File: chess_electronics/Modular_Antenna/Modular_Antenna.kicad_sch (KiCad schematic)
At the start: 11 parts, among them J1 Screw_Terminal_01x16, J2 Conn_02x04_Counter_Clockwise, U1 SN74LV4051AN

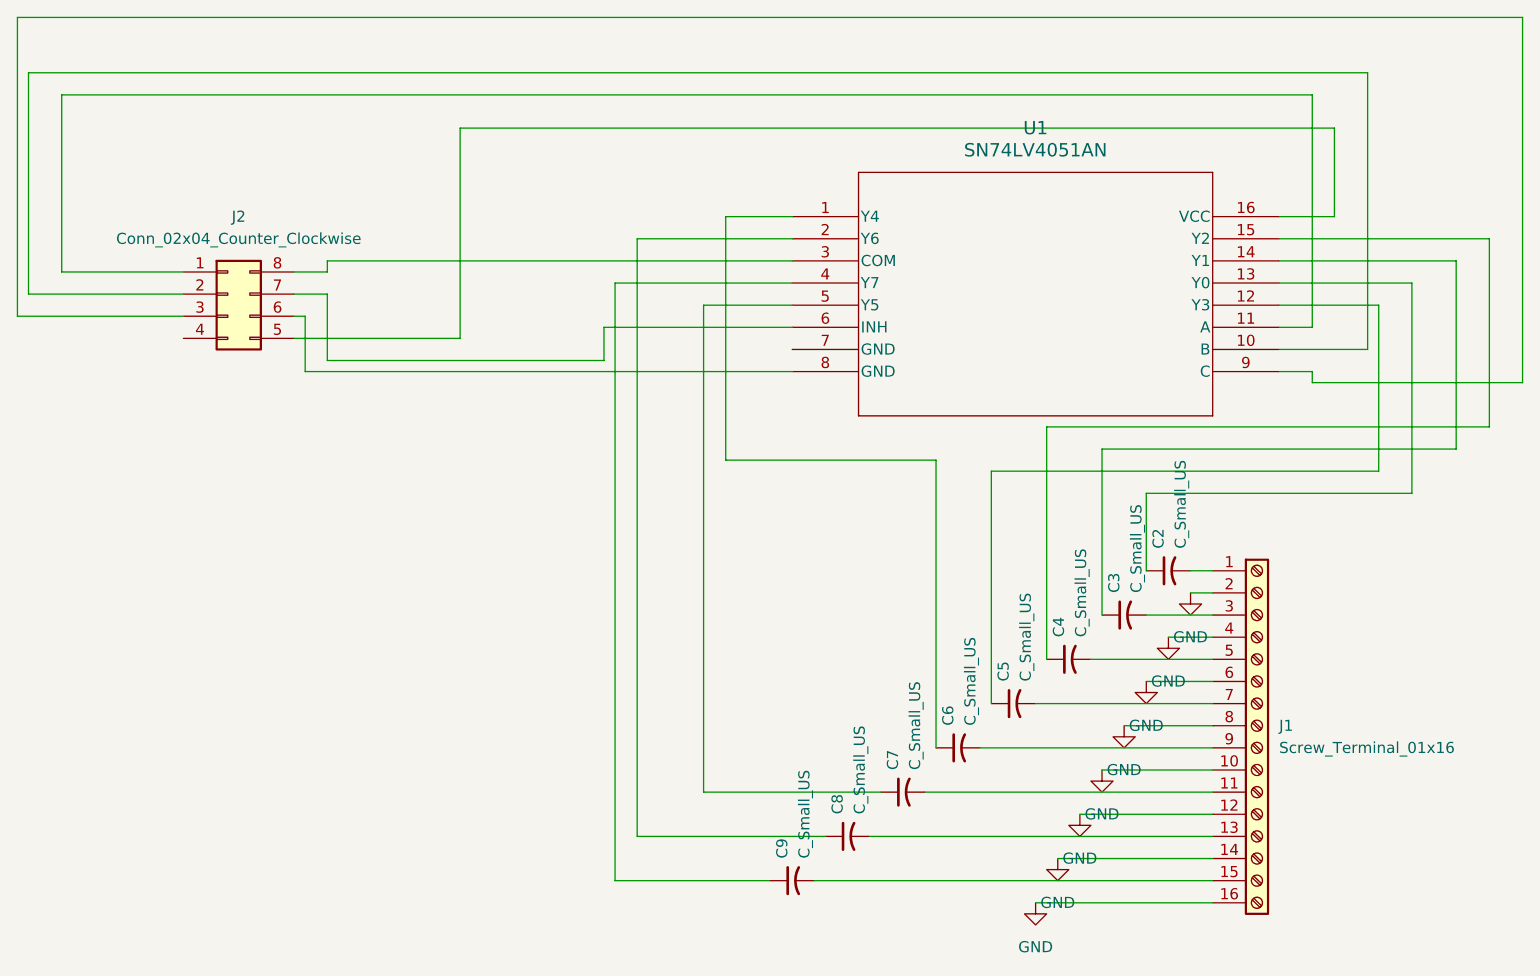
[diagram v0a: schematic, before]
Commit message: Add normally closed relay to modular antenna design
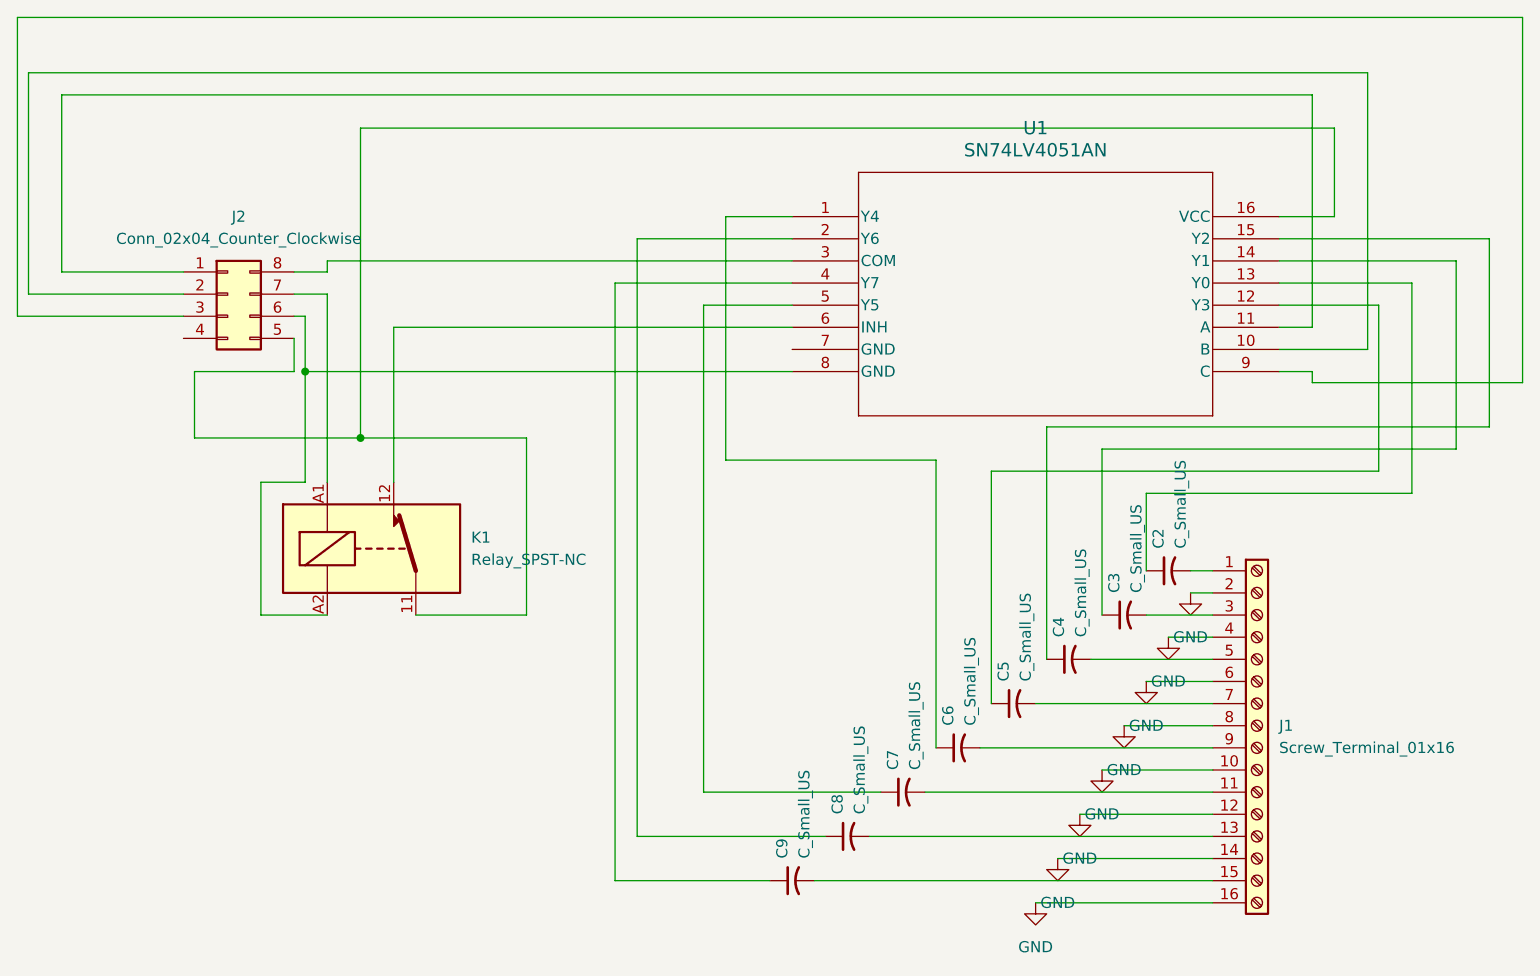
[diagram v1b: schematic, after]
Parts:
- added K1: Relay_SPST-NC, Relay_THT:Relay_SPST_Zettler-AZSR131, symbol Relay:Relay_SPST-NC
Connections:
- net at J2.5 (Pin_5), U1.16 (VCC): now also K1.11
- net at U1.6 (INH): now also K1.12; no longer J2.7 (Pin_7)
- net at J2.6 (Pin_6), U1.8 (GND): now also K1.A2
- new net: J2.7 (Pin_7), K1.A1
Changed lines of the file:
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@@
 	(generator_version "9.0")
 	(paper "A4")
+	(junction
+		(at 55.88 95.25)
+		(diameter 0)
+		(color 0 0 0 0)
+	)
+	(junction
+		(at 49.53 87.63)
+		(diameter 0)
+		(color 0 0 0 0)
+	)
 	(wire
 		(pts
@@
 	(wire
 		(pts
+			(xy 36.83 95.25) (xy 36.83 87.63)
+		)
+		(stroke
+			(width 0)
+			(type default)
+		)
+	)
+	(wire
+		(pts
 			(xy 171.45 53.34) (xy 17.78 53.34)
 		)
@@
 	(wire
 		(pts
+			(xy 55.88 95.25) (xy 74.93 95.25)
+		)
+		(stroke
+			(width 0)
+			(type default)
+		)
+	)
+	(wire
+		(pts
 			(xy 143.51 128.27) (xy 153.67 128.27)
 		)
@@
 	(wire
 		(pts
+			(xy 36.83 87.63) (xy 48.26 87.63)
+		)
+		(stroke
+			(width 0)
+			(type default)
+		)
+	)
+	(wire
+		(pts
 			(xy 151.13 110.49) (xy 153.67 110.49)
 		)
@@
 	(wire
 		(pts
+			(xy 52.07 100.33) (xy 52.07 78.74)
+		)
+		(stroke
+			(width 0)
+			(type default)
+		)
+	)
+	(wire
+		(pts
 			(xy 95.25 80.01) (xy 95.25 135.89)
 		)
@@
 	(wire
 		(pts
-			(xy 52.07 86.36) (xy 52.07 78.74)
-		)
-		(stroke
-			(width 0)
-			(type default)
-		)
-	)
-	(wire
-		(pts
 			(xy 85.09 146.05) (xy 85.09 77.47)
 		)
@@
 	(wire
 		(pts
+			(xy 74.93 115.57) (xy 74.93 95.25)
+		)
+		(stroke
+			(width 0)
+			(type default)
+		)
+	)
+	(wire
+		(pts
 			(xy 146.05 115.57) (xy 153.67 115.57)
 		)
@@
 	(wire
 		(pts
+			(xy 49.53 87.63) (xy 49.53 100.33)
+		)
+		(stroke
+			(width 0)
+			(type default)
+		)
+	)
+	(wire
+		(pts
+			(xy 44.45 100.33) (xy 44.45 115.57)
+		)
+		(stroke
+			(width 0)
+			(type default)
+		)
+	)
+	(wire
+		(pts
+			(xy 59.69 100.33) (xy 59.69 82.55)
+		)
+		(stroke
+			(width 0)
+			(type default)
+		)
+	)
+	(wire
+		(pts
 			(xy 120.65 135.89) (xy 153.67 135.89)
 		)
@@
 	(wire
 		(pts
-			(xy 67.31 59.69) (xy 67.31 83.82)
+			(xy 55.88 59.69) (xy 55.88 95.25)
 		)
 		(stroke
@@
 	(wire
 		(pts
-			(xy 67.31 83.82) (xy 48.26 83.82)
+			(xy 36.83 95.25) (xy 55.88 95.25)
 		)
 		(stroke
@@
 	(wire
 		(pts
+			(xy 48.26 78.74) (xy 52.07 78.74)
+		)
+		(stroke
+			(width 0)
+			(type default)
+		)
+	)
+	(wire
+		(pts
 			(xy 161.29 85.09) (xy 171.45 85.09)
 		)
@@
 	(wire
 		(pts
-			(xy 52.07 86.36) (xy 83.82 86.36)
-		)
-		(stroke
-			(width 0)
-			(type default)
-		)
-	)
-	(wire
-		(pts
 			(xy 167.64 69.85) (xy 167.64 59.69)
 		)
@@
 	(wire
 		(pts
+			(xy 62.23 115.57) (xy 74.93 115.57)
+		)
+		(stroke
+			(width 0)
+			(type default)
+		)
+	)
+	(wire
+		(pts
 			(xy 165.1 87.63) (xy 165.1 88.9)
 		)
@@
 	(wire
 		(pts
-			(xy 52.07 78.74) (xy 48.26 78.74)
-		)
-		(stroke
-			(width 0)
-			(type default)
-		)
-	)
-	(wire
-		(pts
 			(xy 135.89 143.51) (xy 153.67 143.51)
 		)
@@
 	(wire
 		(pts
-			(xy 167.64 59.69) (xy 67.31 59.69)
+			(xy 59.69 82.55) (xy 105.41 82.55)
+		)
+		(stroke
+			(width 0)
+			(type default)
+		)
+	)
+	(wire
+		(pts
+			(xy 167.64 59.69) (xy 55.88 59.69)
 		)
 		(stroke
@@
 	(wire
 		(pts
+			(xy 48.26 87.63) (xy 48.26 83.82)
+		)
+		(stroke
+			(width 0)
+			(type default)
+		)
+	)
+	(wire
+		(pts
 			(xy 87.63 72.39) (xy 105.41 72.39)
 		)
@@
 	(wire
 		(pts
-			(xy 83.82 82.55) (xy 83.82 86.36)
+			(xy 44.45 115.57) (xy 52.07 115.57)
 		)
 		(stroke
@@
 	(wire
 		(pts
+			(xy 49.53 100.33) (xy 44.45 100.33)
+		)
+		(stroke
+			(width 0)
+			(type default)
+		)
+	)
+	(wire
+		(pts
 			(xy 52.07 76.2) (xy 48.26 76.2)
-		)
-		(stroke
-			(width 0)
-			(type default)
-		)
-	)
-	(wire
-		(pts
-			(xy 105.41 82.55) (xy 83.82 82.55)
 		)
 		(stroke
@@
 					(unit 1)
 				)
+			)
+		)
+	)
+	(symbol
+		(lib_id "Relay:Relay_SPST-NC")
+		(at 57.15 107.95 0)
+		(unit 1)
+		(exclude_from_sim no)
+		(in_bom yes)
+		(on_board yes)
+		(dnp no)
+		(fields_autoplaced yes)
+		(property "Reference" "K1"
+			(at 68.58 106.6799 0)
+			(effects
+				(font
+					(size 1.27 1.27)
+				)
+				(justify left)
+			)
+		)
+		(property "Value" "Relay_SPST-NC"
+			(at 68.58 109.2199 0)
+			(effects
+				(font
+					(size 1.27 1.27)
+				)
+				(justify left)
+			)
+		)
+		(property "Footprint" "Relay_THT:Relay_SPST_Zettler-AZSR131"
+			(at 68.58 109.22 0)
+			(effects
+				(font
+					(size 1.27 1.27)
+				)
+				(justify left)
+				(hide yes)
+			)
+		)
+		(property "Datasheet" "~"
+			(at 57.15 107.95 0)
+			(effects
+				(font
+					(size 1.27 1.27)
+				)
+				(hide yes)
+			)
+		)
+		(property "Description" "Relay SPST, normally closed, EN50005"
+			(at 57.15 107.95 0)
+			(effects
+				(font
+					(size 1.27 1.27)
+				)
+				(hide yes)
+			)
+		)
+		(pin "12"
+		)
+		(pin "A2"
+		)
+		(pin "A1"
+		)
+		(pin "11"
+		)
+		(instances
+			(project ""
+				(path "/2162e48e-6969-420a-8380-db6243e992e1"
+					(reference "K1")
+					(unit 1)
+				)
